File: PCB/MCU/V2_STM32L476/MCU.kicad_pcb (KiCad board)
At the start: 2 copper layers, 40 x 46.2 mm, 55 parts, among them IC2 LTC4311CSC6#TRPBF, J1 Conn_02x06_Odd_Even, J2 Conn_02x06_Odd_Even, J5 RESET, J6 Conn_01x04_Pin, Q1 PJE8408_R1_00001, Q2 PJE8408_R1_00001, U1 MB85RS2MTAPNF-G-BDERE1, U3 MAX6372, U4 ADP160AUJZ-3.3-R7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

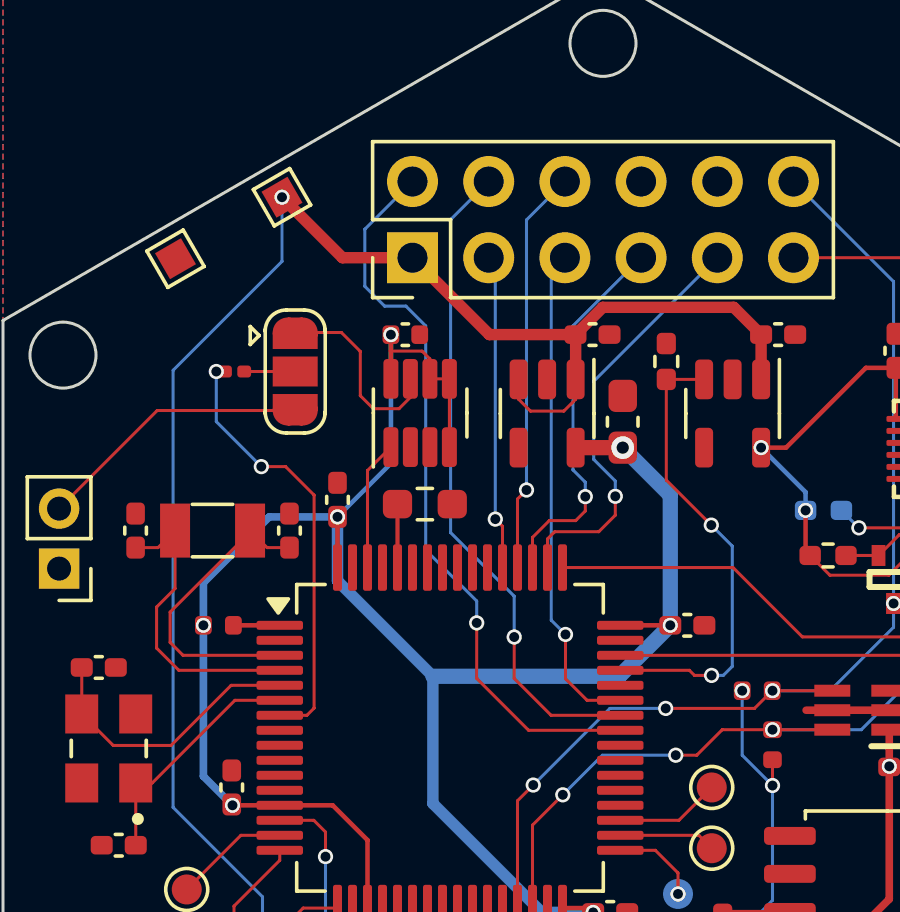
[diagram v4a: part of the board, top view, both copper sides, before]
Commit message: pc:finished L476 MCU board
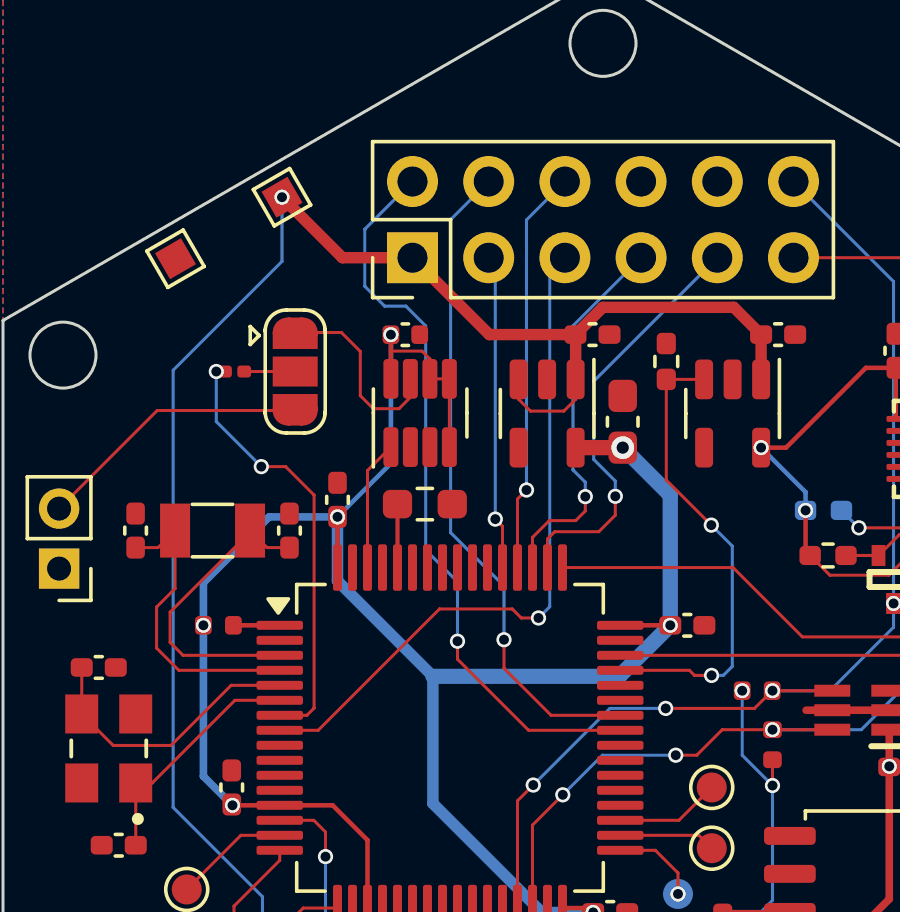
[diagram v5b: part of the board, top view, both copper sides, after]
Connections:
- J1 pad 5: PA10 -> PC0
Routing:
- net PC0: track 0.00 -> 22.8 mm, vias 0 -> 1
- net PA10: track 16.5 -> 0.00 mm, vias 1 -> 0
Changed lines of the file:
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@@
 			(layers "*.Cu" "*.Mask")
 			(remove_unused_layers no)
-			(net 68 "PA10")
+			(net 60 "PC0")
 			(pinfunction "Pin_5")
 			(pintype "passive")
@@
 	)
 	(segment
+		(start 144.71 98.173621)
+		(end 147.135 98.173621)
+		(width 0.1016)
+		(layer "F.Cu")
+		(net 60)
+	)
+	(segment
+		(start 140.665 102.218621)
+		(end 144.71 98.173621)
+		(width 0.1016)
+		(layer "F.Cu")
+		(net 60)
+	)
+	(segment
+		(start 147.435 98.473621)
+		(end 148.01 98.473621)
+		(width 0.1016)
+		(layer "F.Cu")
+		(net 60)
+	)
+	(segment
+		(start 147.135 98.173621)
+		(end 147.435 98.473621)
+		(width 0.1016)
+		(layer "F.Cu")
+		(net 60)
+	)
+	(segment
+		(start 139.385 102.218621)
+		(end 140.665 102.218621)
+		(width 0.1016)
+		(layer "F.Cu")
+		(net 60)
+	)
+	(via
+		(at 148.01 98.473621)
+		(size 0.508)
+		(drill 0.3302)
+		(layers "F.Cu" "B.Cu")
+		(net 60)
+	)
+	(segment
+		(start 148.01 98.473621)
+		(end 148.385 98.098621)
+		(width 0.1016)
+		(layer "B.Cu")
+		(net 60)
+	)
+	(segment
+		(start 148.385 98.098621)
+		(end 148.385 86.970599)
+		(width 0.1016)
+		(layer "B.Cu")
+		(net 60)
+	)
+	(segment
+		(start 148.385 86.970599)
+		(end 148.89 86.465599)
+		(width 0.1016)
+		(layer "B.Cu")
+		(net 60)
+	)
+	(segment
 		(start 146.815 110.373621)
 		(end 145.81 109.368621)
@@
 	)
 	(segment
-		(start 150.735 101.718621)
-		(end 148.43 101.718621)
+		(start 146.86 99.198621)
+		(end 146.86 100.148621)
 		(width 0.1016)
 		(layer "F.Cu")
@@
 	(segment
 		(start 148.43 101.718621)
-		(end 147.2 100.488621)
+		(end 150.735 101.718621)
 		(width 0.1016)
 		(layer "F.Cu")
@@
 	)
 	(segment
-		(start 147.2 100.488621)
-		(end 147.2 99.108621)
+		(start 146.86 100.148621)
+		(end 148.43 101.718621)
 		(width 0.1016)
 		(layer "F.Cu")
@@
 	)
 	(via
-		(at 147.2 99.108621)
+		(at 146.86 99.198621)
 		(size 0.508)
 		(drill 0.3302)
@@
 	(segment
 		(start 145.08 95.628621)
-		(end 147.2 97.748621)
+		(end 145.08 85.195599)
 		(width 0.1016)
 		(layer "B.Cu")
@@
 	)
 	(segment
-		(start 147.2 97.748621)
-		(end 147.2 99.108621)
+		(start 145.08 85.195599)
+		(end 146.35 83.925599)
 		(width 0.1016)
 		(layer "B.Cu")
@@
 	)
 	(segment
-		(start 146.35 83.925599)
-		(end 145.08 85.195599)
+		(start 146.86 99.198621)
+		(end 146.86 97.408621)
 		(width 0.1016)
 		(layer "B.Cu")
@@
 	)
 	(segment
-		(start 145.08 85.195599)
+		(start 146.86 97.408621)
 		(end 145.08 95.628621)
 		(width 0.1016)
@@
 	)
 	(segment
-		(start 148.91 99.023621)
-		(end 148.91 100.498621)
-		(width 0.1016)
-		(layer "F.Cu")
-		(net 68)
-	)
-	(segment
-		(start 149.63 101.218621)
-		(end 150.735 101.218621)
-		(width 0.1016)
-		(layer "F.Cu")
-		(net 68)
-	)
-	(segment
-		(start 148.91 100.498621)
-		(end 149.63 101.218621)
-		(width 0.1016)
-		(layer "F.Cu")
-		(net 68)
-	)
-	(via
-		(at 148.91 99.023621)
-		(size 0.508)
-		(drill 0.3302)
-		(layers "F.Cu" "B.Cu")
-		(net 68)
-	)
-	(segment
-		(start 148.89 86.465599)
-		(end 148.435 86.920599)
-		(width 0.1016)
-		(layer "B.Cu")
-		(net 68)
-	)
-	(segment
-		(start 148.435 86.920599)
-		(end 148.435 98.548621)
-		(width 0.1016)
-		(layer "B.Cu")
-		(net 68)
-	)
-	(segment
-		(start 148.435 98.548621)
-		(end 148.91 99.023621)
-		(width 0.1016)
-		(layer "B.Cu")
-		(net 68)
-	)
-	(segment
 		(start 147.475 112.328621)
 		(end 148.89 113.743621)
@@
 	)
 	(segment
-		(start 145.95 98.638621)
-		(end 145.95 100.488621)
+		(start 145.31 99.848621)
+		(end 147.68 102.218621)
 		(width 0.1016)
 		(layer "F.Cu")
@@
 	)
 	(segment
-		(start 145.95 100.488621)
-		(end 147.68 102.218621)
+		(start 145.31 99.248621)
+		(end 145.31 99.848621)
 		(width 0.1016)
 		(layer "F.Cu")
@@
 	)
 	(via
-		(at 145.95 98.638621)
+		(at 145.31 99.248621)
 		(size 0.508)
 		(drill 0.3302)
@@
 	)
 	(segment
-		(start 145.95 98.638621)
-		(end 145.95 97.908621)
+		(start 142.88 88.078621)
+		(end 142.22 87.418621)
 		(width 0.1016)
 		(layer "B.Cu")
@@
 	)
 	(segment
-		(start 142.22 87.418621)
-		(end 142.22 85.515599)
+		(start 144.25 88.738621)
+		(end 143.59 88.078621)
 		(width 0.1016)
 		(layer "B.Cu")
@@
 	)
 	(segment
-		(start 144.25 88.738621)
-		(end 143.59 88.078621)
+		(start 142.22 87.418621)
+		(end 142.22 85.515599)
 		(width 0.1016)
 		(layer "B.Cu")
@@
 	)
 	(segment
-		(start 142.22 85.515599)
-		(end 143.81 83.925599)
+		(start 144.25 96.208621)
+		(end 144.25 88.738621)
 		(width 0.1016)
 		(layer "B.Cu")
@@
 	)
 	(segment
-		(start 142.88 88.078621)
-		(end 142.22 87.418621)
+		(start 143.59 88.078621)
+		(end 142.88 88.078621)
 		(width 0.1016)
 		(layer "B.Cu")
@@
 	)
 	(segment
-		(start 144.25 96.208621)
-		(end 144.25 88.738621)
+		(start 145.31 97.268621)
+		(end 144.25 96.208621)
 		(width 0.1016)
 		(layer "B.Cu")
@@
 	)
 	(segment
-		(start 145.95 97.908621)
-		(end 144.25 96.208621)
+		(start 145.31 99.248621)
+		(end 145.31 97.268621)
 		(width 0.1016)
 		(layer "B.Cu")
@@
 	)
 	(segment
-		(start 143.59 88.078621)
-		(end 142.88 88.078621)
+		(start 142.22 85.515599)
+		(end 143.81 83.925599)
 		(width 0.1016)
 		(layer "B.Cu")

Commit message: mac: finishing the L476 mcu board design rule checking
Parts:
- moved C17 0.11 mm to (141.4, 94.5)
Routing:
- net +3.3V: track 122.8 -> 127.1 mm, vias 13 -> 12
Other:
- board text added: "HexSense STM32L476_MCU"
- board text removed: "HexSense L476_MCU"

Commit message: mac: finishing the L476 mcu board design rule checking
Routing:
- net GND: vias 2 -> 51

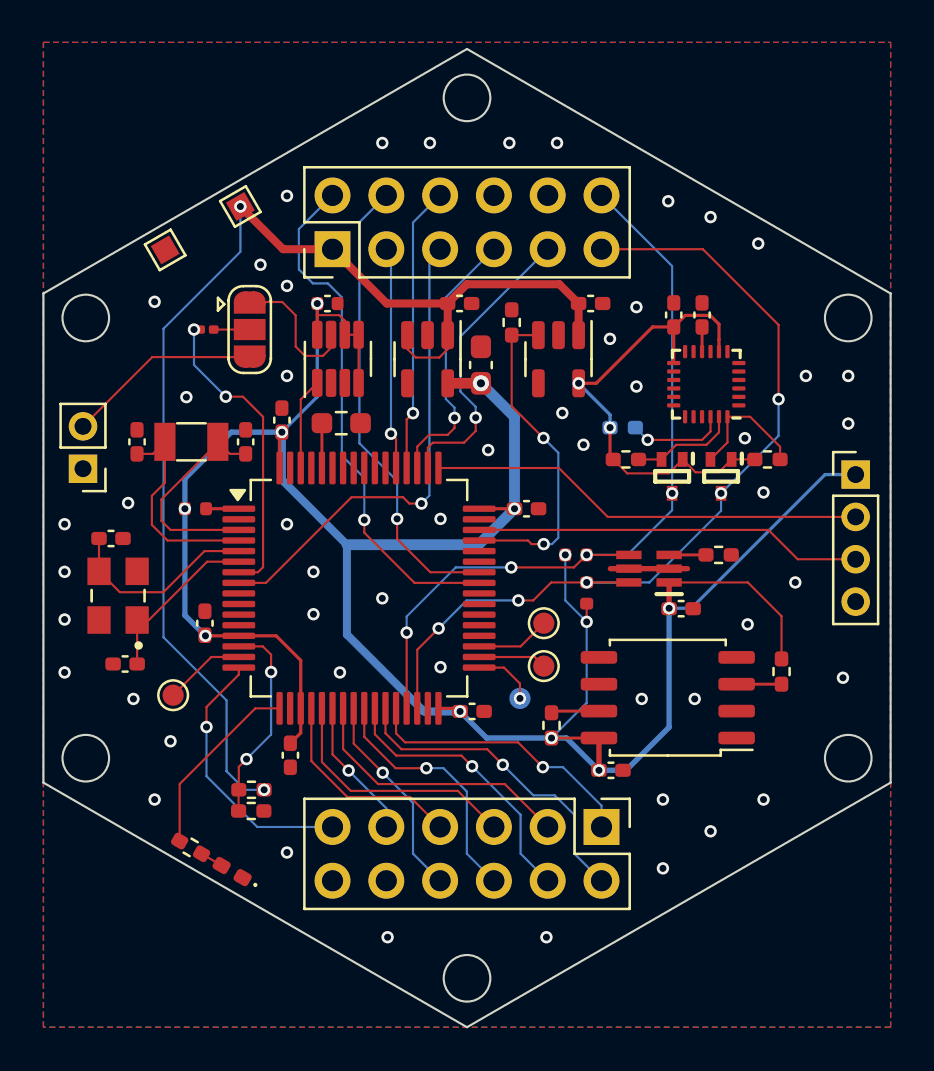
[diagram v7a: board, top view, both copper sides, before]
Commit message: mac:working on esp32s3 mcu brd, forgot the strapping pins.
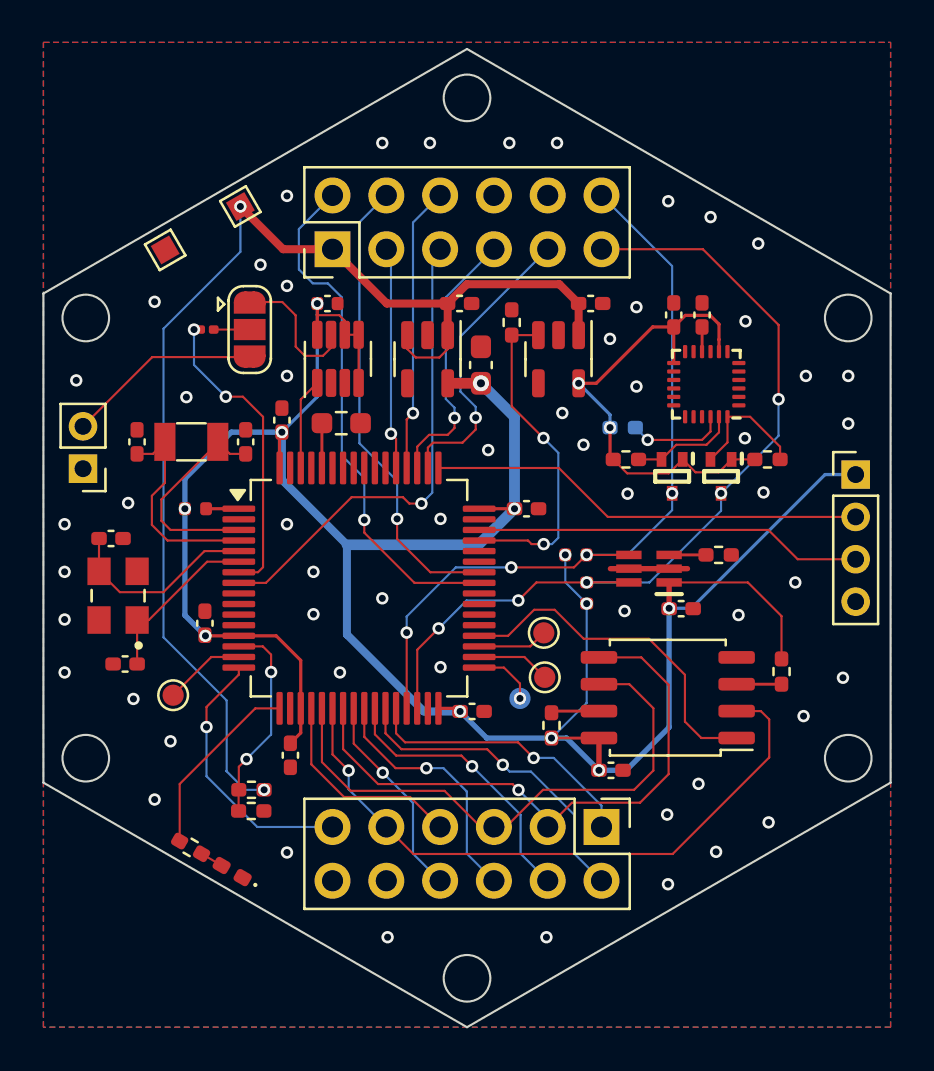
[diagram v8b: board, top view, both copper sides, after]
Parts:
- moved TP5 0.53 mm to (153.8, 106.7)
- moved TP6 0.45 mm to (153.8, 104.6)
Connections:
- U1 pad 1: /D6 -> PB15
- U1 pad 2: /MISO -> SPI1_MISO
- U1 pad 5: /MOSI -> SPI1_MOSI
- U1 pad 6: /SCK -> SPI1_SCK
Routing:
- net SPI1_MISO: track 6.65 -> 30.6 mm
- net PB15: track 0.00 -> 16.5 mm
- net SPI1_MOSI: track 13.1 -> 28.1 mm, vias 0 -> 1
- net SPI1_SCK: track 11.9 -> 26.5 mm
- net +3.3V: track 127.1 -> 126.2 mm
- net GND: vias 51 -> 55
